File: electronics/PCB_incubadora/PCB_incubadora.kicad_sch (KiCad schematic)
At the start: 14 parts, among them J1 HDR-4x1, J10 HDR-2x1, J11 HDR-2x1, J2 HDR-4x1, J3 HDR-2x1, J4 HDR-4x1, J5 HDR-5x1, J6 Conn_02x04_Odd_Even, J7 HDR-4x1, J8 Conn_02x04_Odd_Even, J9 HDR-2x1, X1 ESP32-DevKit, X2 EasyDriver, X3 DC-DC

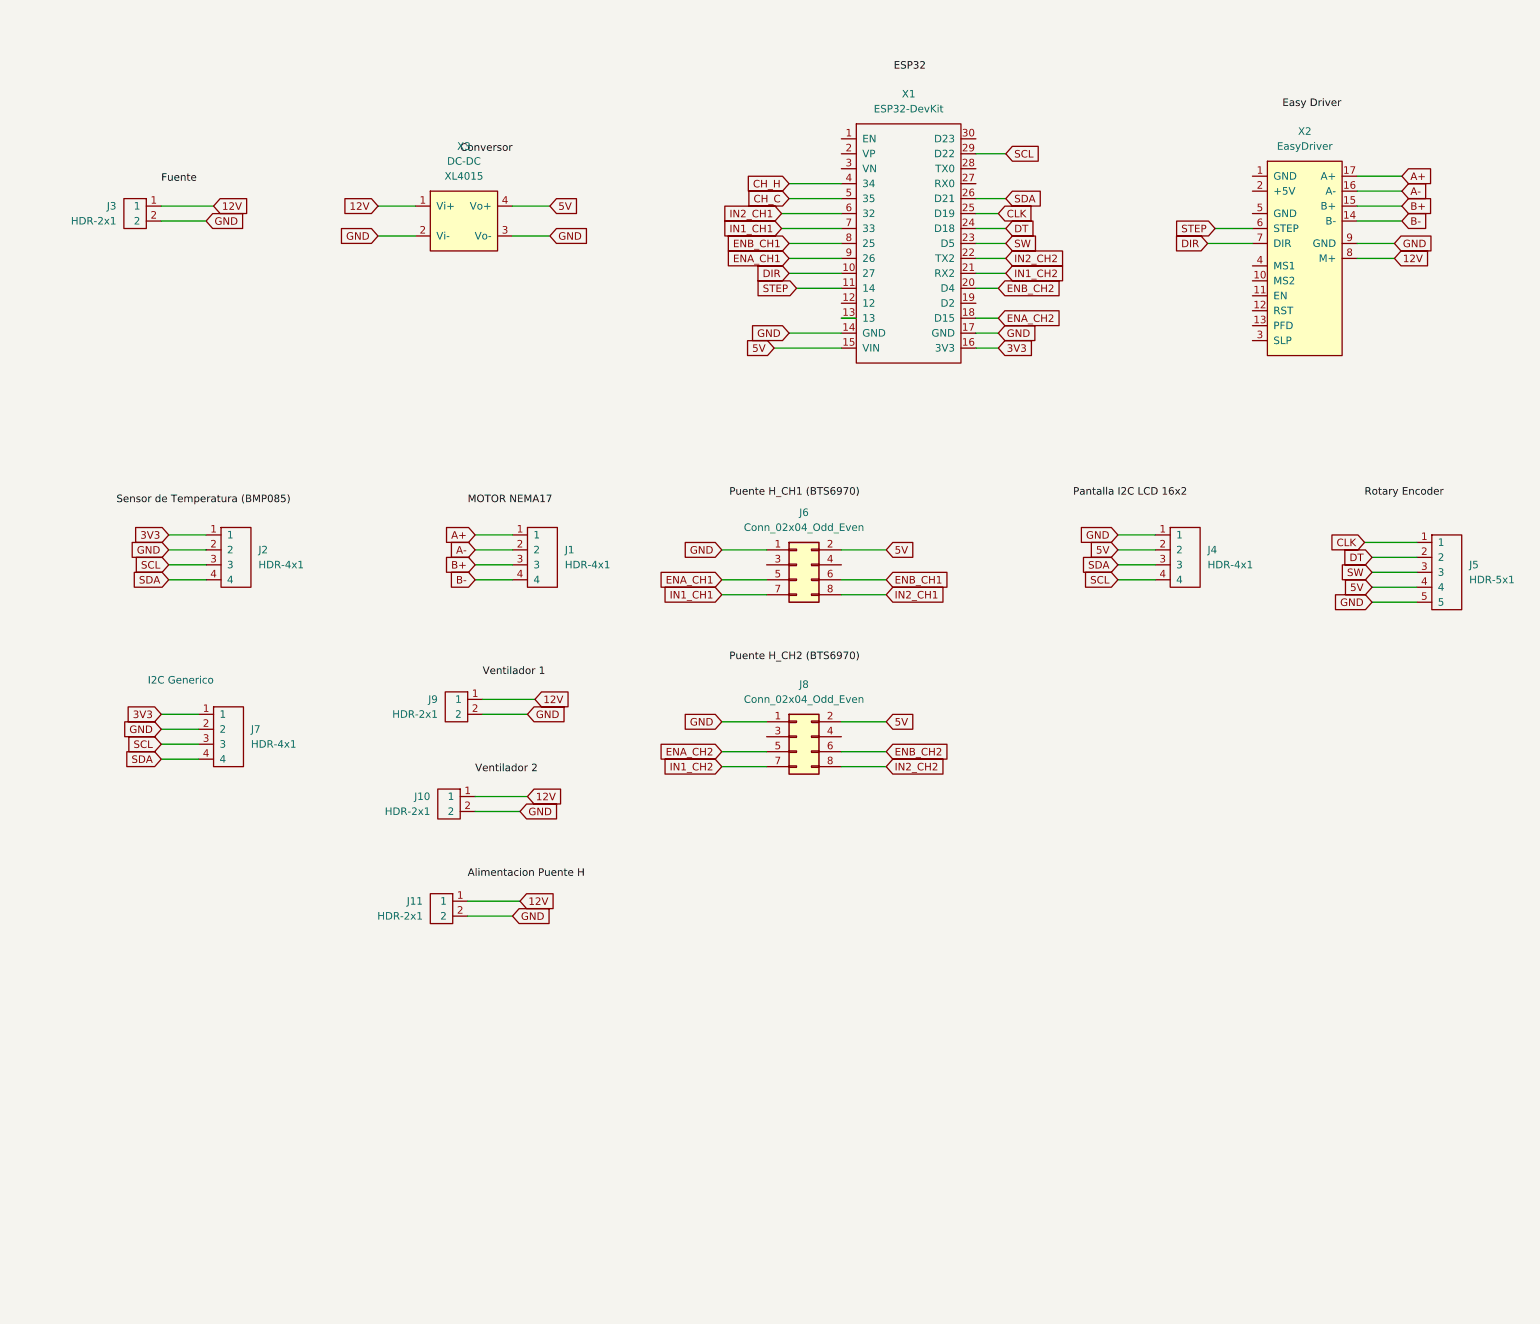
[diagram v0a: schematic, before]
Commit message: updating 3d model of pcb
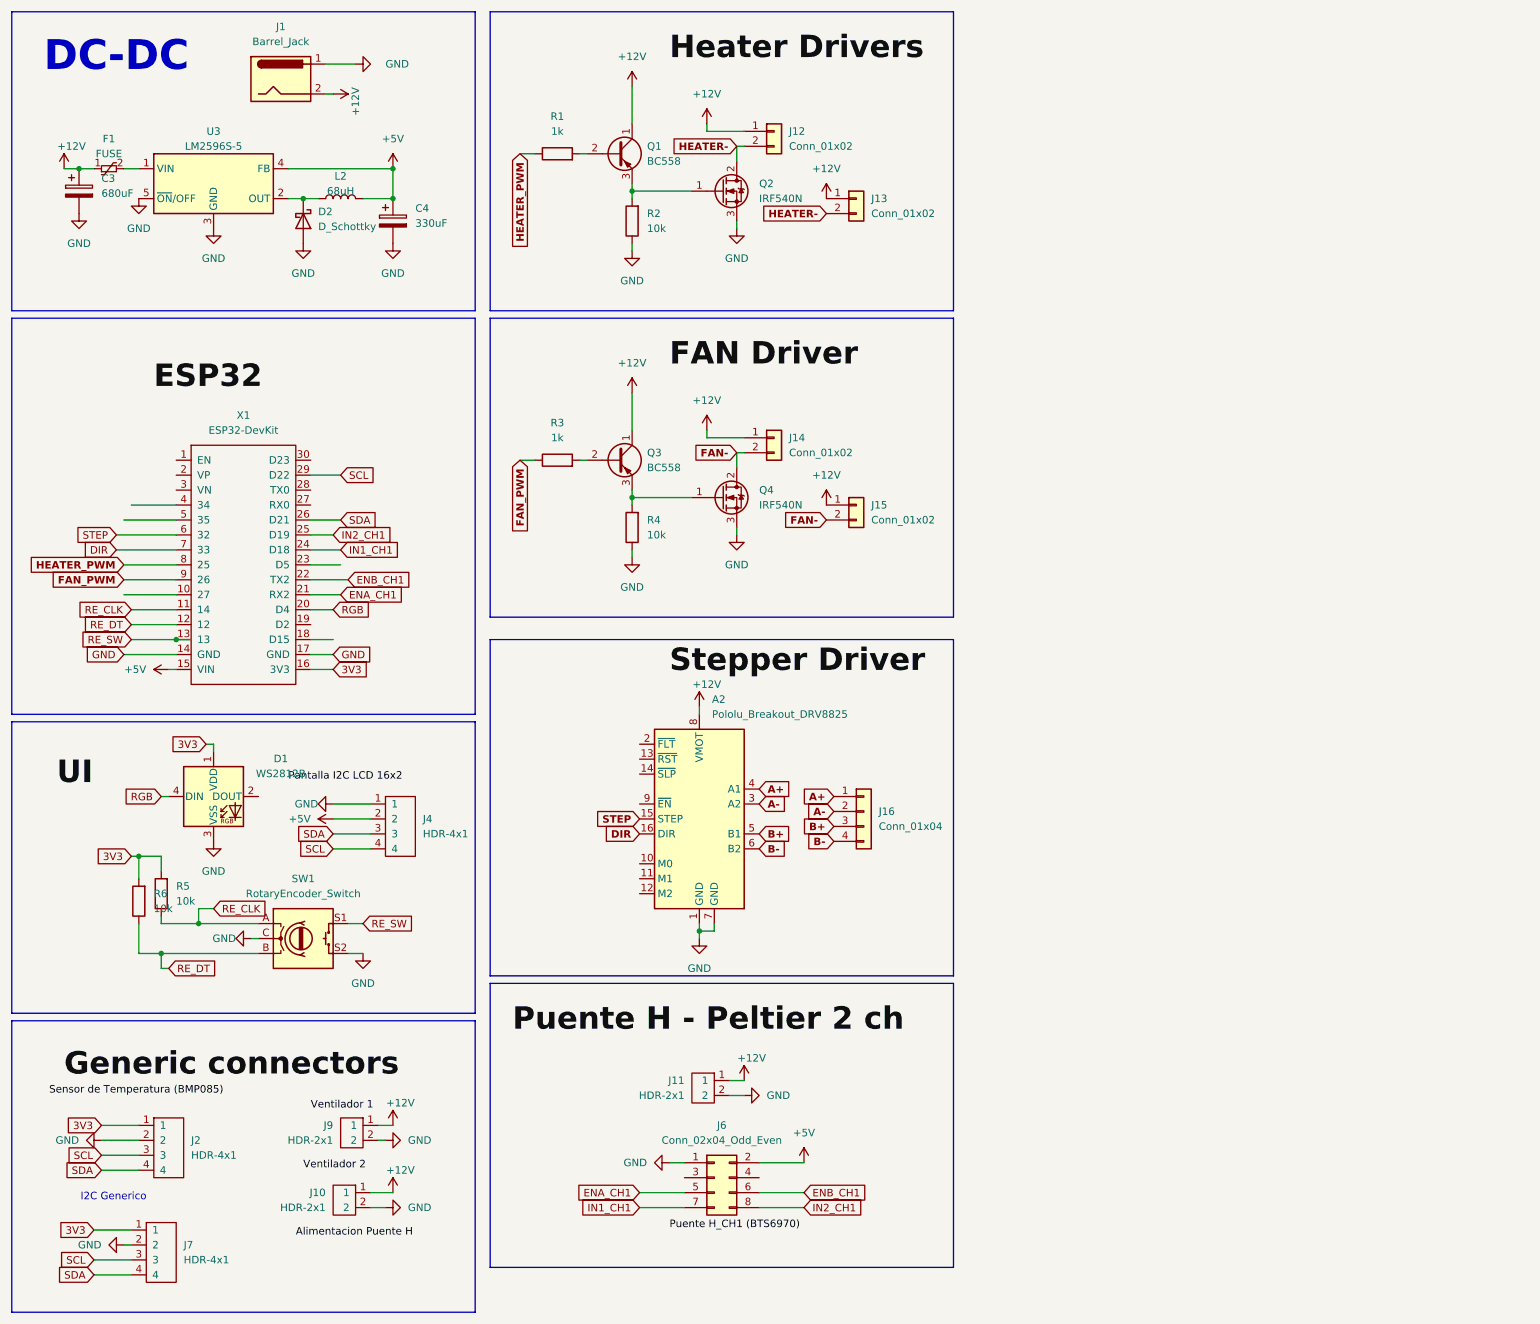
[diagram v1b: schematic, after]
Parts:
- removed J1: HDR-4x1, Connector_PinHeader_2.54mm:PinHeader_1x04_P2.54mm_Vertical, symbol IoWLabsConnectors:HDR-4x1
- removed J3: HDR-2x1, Connector_PinHeader_2.54mm:PinHeader_1x02_P2.54mm_Vertical, symbol IoWLabsConnectors:HDR-2x1
- removed J5: HDR-5x1, Connector_PinHeader_2.54mm:PinHeader_1x05_P2.54mm_Vertical, symbol IoWLabsConnectors:HDR-5x1
- removed J8: Conn_02x04_Odd_Even, Connector_PinHeader_2.54mm:PinHeader_2x04_P2.54mm_Vertical, symbol Connector_Generic:Conn_02x04_Odd_Even
- removed X2: EasyDriver, IoWLabsModules:EasyDriver, symbol IoWLabsModules:EasyDriver
- removed X3: DC-DC, IoWLabsModules:LM2596, symbol IoWLabsModules:DC-DC
- added A2: Pololu_Breakout_DRV8825, Module:Pololu_Breakout-16_15.2x20.3mm, symbol Driver_Motor:Pololu_Breakout_DRV8825
- added C3: 680uF, Capacitor_SMD:CP_Elec_10x10, symbol Device:C_Polarized
- added C4: 330uF, Capacitor_SMD:CP_Elec_10x10, symbol Device:C_Polarized
- added D1: WS2812B, LED_SMD:LED_WS2812B_PLCC4_5.0x5.0mm_P3.2mm, symbol LED:WS2812B
- added D2: D_Schottky, Diode_SMD:D_SMB_Handsoldering, symbol Device:D_Schottky
- added F1: FUSE, Fuse:Fuse_1206_3216Metric, symbol IoWLabs:FUSE
- added J1: Barrel_Jack, Connector_BarrelJack:BarrelJack_Horizontal, symbol Connector:Barrel_Jack
- added J12, J13, J14, J15: Conn_01x02, TerminalBlock_4Ucon:TerminalBlock_4Ucon_1x02_P3.50mm_Horizontal, symbol Connector_Generic:Conn_01x02
- added J16: Conn_01x04, TerminalBlock_4Ucon:TerminalBlock_4Ucon_1x04_P3.50mm_Horizontal, symbol Connector_Generic:Conn_01x04
- added L2: 68uH, Inductor_SMD:L_12x12mm_H6mm, symbol Device:L
- added Q1, Q3: BC558, Package_TO_SOT_THT:TO-92_Inline, symbol Transistor_BJT:BC558
- added Q2, Q4: IRF540N, Package_TO_SOT_THT:TO-220-3_Vertical, symbol Transistor_FET:IRF540N
- added R1, R3: 1k, Resistor_SMD:R_0603_1608Metric, symbol Device:R
- added R2, R4, R5, R6: 10k, Resistor_SMD:R_0603_1608Metric, symbol Device:R
- added SW1: RotaryEncoder_Switch, Rotary_Encoder:RotaryEncoder_Alps_EC11E-Switch_Vertical_H20mm, symbol Device:RotaryEncoder_Switch
- added U3: LM2596S-5, Package_TO_SOT_SMD:TO-263-5_TabPin3, symbol Regulator_Switching:LM2596S-5
- J10, J11, J9: footprint Connector_PinHeader_2.54mm:PinHeader_1x02_P2.54mm_Vertical -> TerminalBlock_4Ucon:TerminalBlock_4Ucon_1x02_P3.50mm_Horizontal
- J2, J7: footprint Connector_PinHeader_2.54mm:PinHeader_1x04_P2.54mm_Vertical -> Connector_JST:JST_XH_B4B-XH-A_1x04_P2.50mm_Vertical
- J4: footprint Connector_PinHeader_2.54mm:PinHeader_1x04_P2.54mm_Vertical -> IoWLabsModules:OLED 0'96 SPI module
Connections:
- net CLK is gone; now on net IN2_CH1: X1.25 (D19)
- net DT is gone; now on net IN1_CH1: X1.24 (D18)
- net IN1_CH2 is gone; now on net ENA_CH1: X1.21 (RX2)
- net IN2_CH2 is gone; now on net ENB_CH1: X1.22 (TX2)
- net 3V3: now also D1.1 (VDD), R5.2, R6.2
- net A+: now also A2.4 (A1), J16.1 (Pin_1)
- net A-: now also A2.3 (A2), J16.2 (Pin_2)
- net B+: now also A2.5 (B1), J16.3 (Pin_3)
- net B-: now also A2.6 (B2), J16.4 (Pin_4)
- net DIR: now also X1.7 (33), A2.16 (DIR); no longer X1.10 (27)
- net ENA_CH1: no longer X1.9 (26)
- net ENB_CH1: no longer X1.8 (25)
- net GND: now also A2.1 (GND), A2.7 (GND), C3.2, C4.2, D1.3 (VSS), D2.2 (A), J1.1, Q2.3 (S), Q4.3 (S), R2.1, R4.1, SW1.C, SW1.S2, U3.3 (GND), U3.5 (~{ON}/OFF)
- net IN1_CH1: no longer X1.7 (33)
- net IN2_CH1: no longer X1.6 (32)
- net STEP: now also X1.6 (32), A2.15 (STEP); no longer X1.11 (14)
- net RE_DT: now reaches X1.12
- net RE_DT: now also R6.1, SW1.B
- net RE_SW: now reaches X1.13
- net RE_SW: now also SW1.S1
- net 12V renamed +12V
- net +12V: now also A2.8 (VMOT), C3.1, F1.1, J1.2, J12.1 (Pin_1), J13.1 (Pin_1), J14.1 (Pin_1), J15.1 (Pin_1), Q1.1 (C), Q3.1 (C)
- net 5V renamed +5V
- net +5V: now also C4.1, L2.2, U3.4 (FB)
- net CH_C: no longer names the net of X1.5 (35)
- net CH_H: no longer names the net of X1.4 (34)
- net ENA_CH2: no longer names the net of X1.18 (D15)
- net ENB_CH2 renamed RGB
- net RGB: now also D1.4 (DIN)
- net SW: no longer names the net of X1.23 (D5)
- new net: F1.2, U3.1 (VIN)
- new net: Q3.3 (E), Q4.1 (G), R4.2
- new net: Q1.3 (E), Q2.1 (G), R2.2
- new net: Q3.2 (B), R3.2
- new net: D2.1 (K), L2.1, U3.2 (OUT)
- new net: Q1.2 (B), R1.2
- new net FAN-: J14.2 (Pin_2), J15.2 (Pin_2), Q4.2 (D)
- new net FAN_PWM: R3.1, X1.9 (26)
- new net HEATER-: J12.2 (Pin_2), J13.2 (Pin_2), Q2.2 (D)
- new net HEATER_PWM: R1.1, X1.8 (25)
- new net RE_CLK: R5.1, SW1.A, X1.11 (14)
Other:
- note added: "DC-DC"
- moved on the sheet: J10, J11, J2, J4, J6, J7, J9, X1

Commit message: updating pcb
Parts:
- added J3: Conn_01x03, symbol Connector_Generic:Conn_01x03
- added R7: 4.7K, Resistor_SMD:R_0603_1608Metric, symbol Device:R
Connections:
- net 3V3: now also J3.1 (Pin_1), R7.2
- net GND: now also J3.3 (Pin_3)
- net TS_PIN: now reaches X1.10 (27)
- net TS_PIN: now also J3.2 (Pin_2), R7.1
